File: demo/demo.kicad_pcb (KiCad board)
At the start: 2 copper layers, 50 x 35 mm, 18 parts, among them J1 Conn_01x04, Q1 BSS138, SW1 Reset, U1 ATtiny85, Y1 16MHz

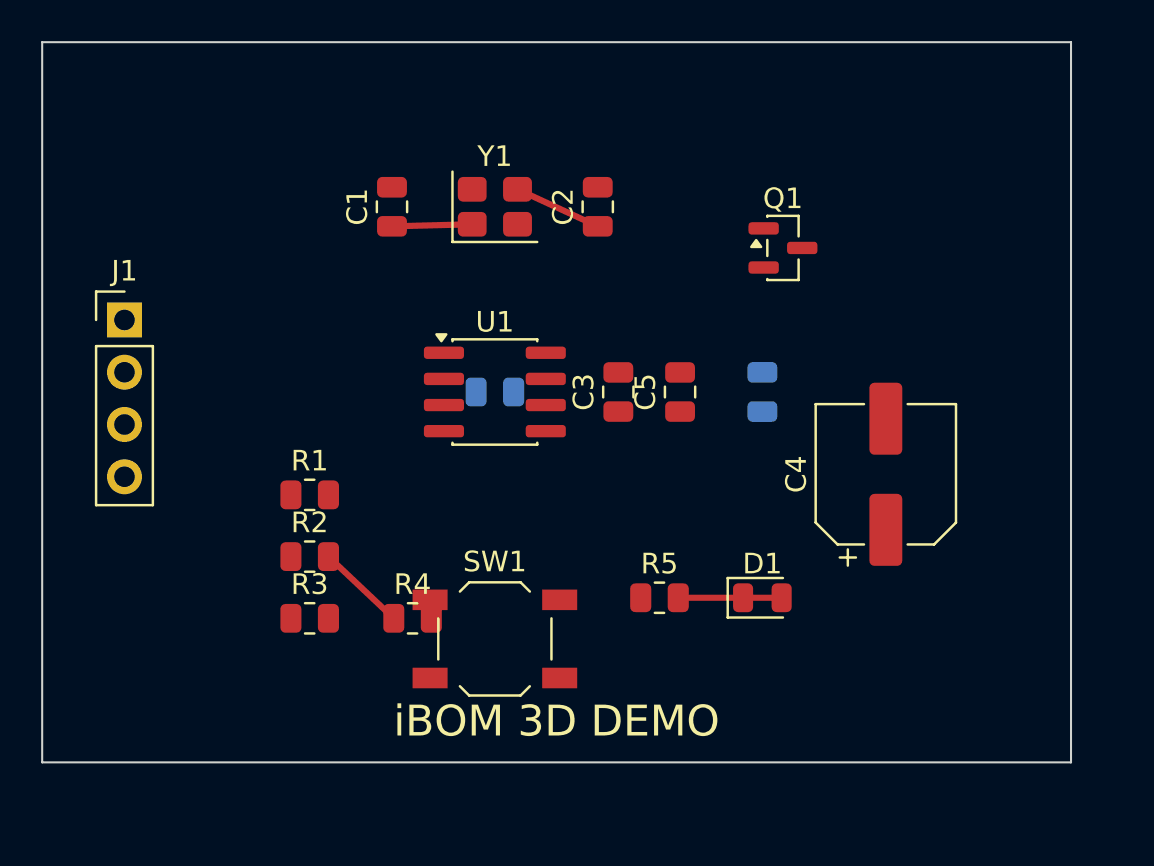
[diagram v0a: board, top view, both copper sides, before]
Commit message: Demo board: DRC-clean placement, autorouted, rounded corners
The first board failed DRC: a courtyard overlap, two shorts, two
solder-mask bridges and seven silkscreen violations. Parts are now
spread out and the outline has 3 mm corner radii.

Routed with Freerouting 2.4.1 (all 39 connections, 128 segments, 16
vias). It necks a few segments down to 0.15 mm between pads, so the
board's minimum track width is 0.15 mm. kicad-cli pcb drc
--severity-all now reports 0 violations and 0 unconnected items.

build.sh also exports tracks into the GLB, so the routing shows in 3D.

Co-Authored-By: Claude Opus 5.5 (1M context) <noreply@anthropic.com>
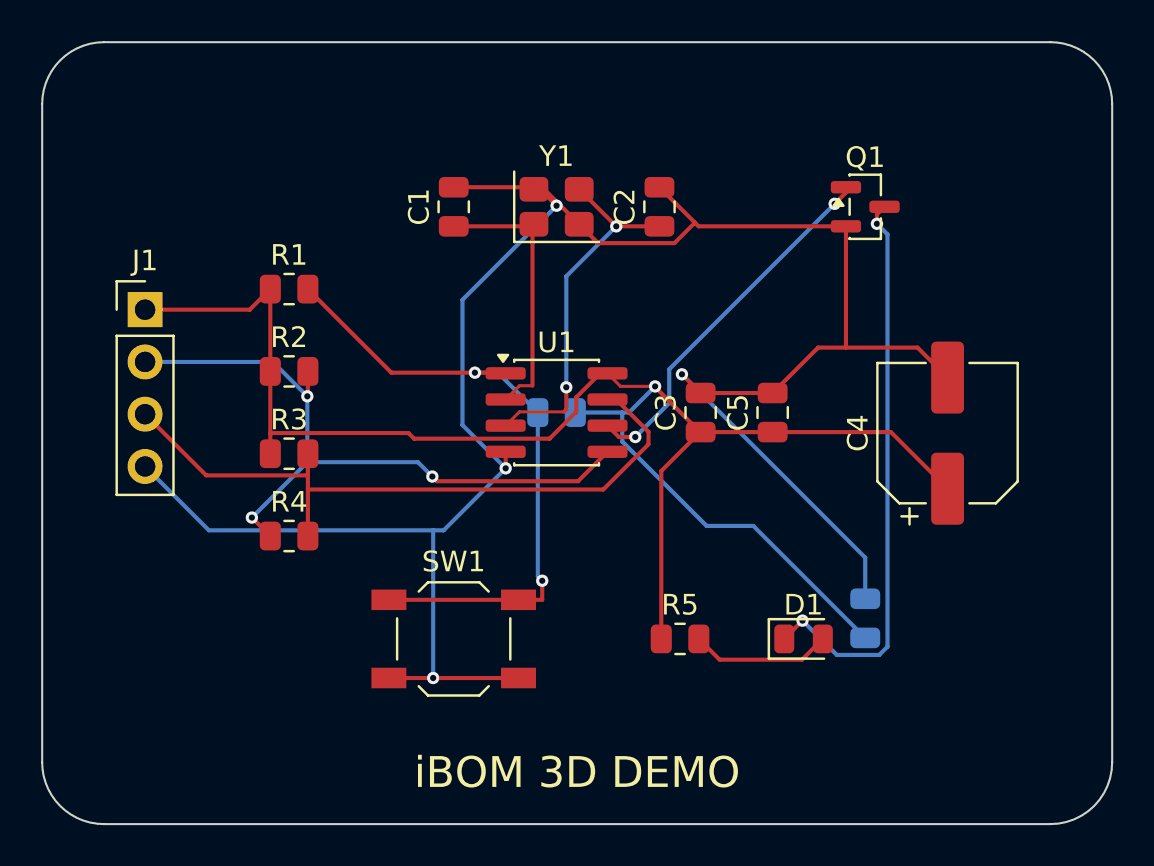
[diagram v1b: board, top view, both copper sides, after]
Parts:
- moved C6 12.1 mm to (40.0, 28.0)
- moved R1 10.0 mm to (12.0, 12.0)
- moved R2 9.06 mm to (12.0, 16.0)
- moved R3 8.06 mm to (12.0, 20.0)
- moved R4 7.21 mm to (12.0, 24.0)
- moved C5 4.61 mm to (35.5, 18.0)
- moved Q1 4.47 mm to (40.0, 8.00)
- moved C3 4.12 mm to (32.0, 18.0)
- moved C4 3.61 mm to (44.0, 19.0)
- moved R6 3.16 mm to (25.0, 18.0)
- moved U1 3.16 mm to (25.0, 18.0)
- moved C1 3.00 mm to (20.0, 8.00)
- moved C2 3.00 mm to (30.0, 8.00)
- moved Y1 3.00 mm to (25.0, 8.00)
- moved D1 2.83 mm to (37.0, 29.0)
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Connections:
- D1 pad 1: GND -> LED_K
- Q1 pad 1: (no net) -> LED
- Q1 pad 2: (no net) -> GND
- Q1 pad 3: VCC -> LED_K
- R5 pad 1: LED -> VCC
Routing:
- net GND: track 0.00 -> 109.7 mm, vias 0 -> 4
- net VCC: track 0.00 -> 84.0 mm, vias 0 -> 1
- net SCL: track 0.00 -> 33.9 mm
- net RST: track 0.00 -> 31.8 mm, vias 0 -> 2
- net SDA: track 4.37 -> 33.6 mm, vias 0 -> 3
- net LED_K: track 0.00 -> 28.0 mm, vias 0 -> 2
- net LED: track 0.00 -> 18.0 mm, vias 0 -> 2
- net XTAL2: track 4.30 -> 17.8 mm, vias 0 -> 2
- net XTAL1: track 3.90 -> 13.3 mm
- net LED_A: track 5.02 -> 6.86 mm
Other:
- board size 50 x 35 mm -> 52 x 38 mm

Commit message: Demo board: Manufacturer/MPN on every part; R7 is DNP only by value
Every part now carries real Manufacturer and MPN fields (hidden, on the
Fab layer, so nothing lands on the silkscreen).

R7 ("10k DNP", 0805, LED_K to GND) is DNP only through its value, so the
demo shows the WARNING badge from #29 next to the two parts that use
KiCad's DNP property (R4, C5).

R7 routed with Freerouting; kicad-cli pcb drc --severity-all reports 0
violations and 0 unconnected items.

Fixes #28

Co-Authored-By: Claude Opus 5.5 (1M context) <noreply@anthropic.com>
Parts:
- added R7: 10k DNP, R_0805_2012Metric, F.Cu at (46.0, 29.0)
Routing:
- net LED_K: track 28.0 -> 37.9 mm
- net GND: track 109.7 -> 117.4 mm, vias 4 -> 5

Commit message: WARNING badge after the value; demo R7's value is just "DNP"
The yellow WARNING badge now follows the value in the Value cell
instead of preceding it. The demo's R7 carries the bare value "DNP".

Co-Authored-By: Claude Opus 5.5 (1M context) <noreply@anthropic.com>
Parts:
- R7: value 10k DNP -> DNP
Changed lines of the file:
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@@
 			)
 		)
-		(property "Value" "10k DNP"
+		(property "Value" "DNP"
 			(at 0 1.65 90)
 			(layer "F.Fab")
